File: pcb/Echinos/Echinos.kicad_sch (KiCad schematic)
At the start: 1 part

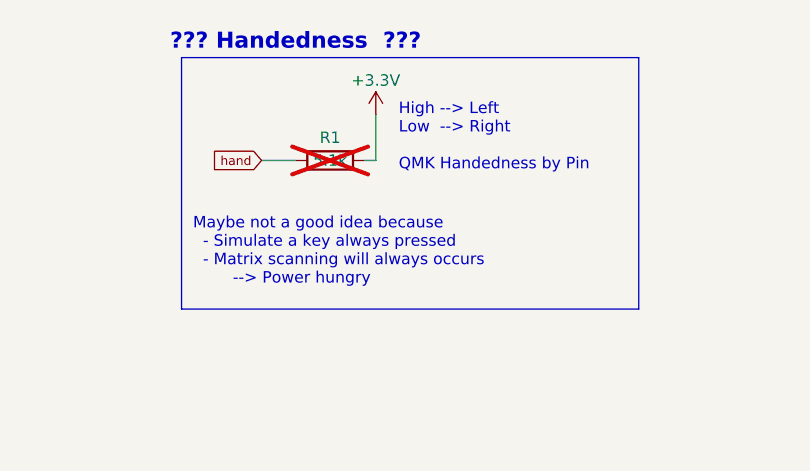
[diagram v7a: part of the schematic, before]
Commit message: [PCB] - Save last state with Gemini MCU board (with mod exposing more pins).
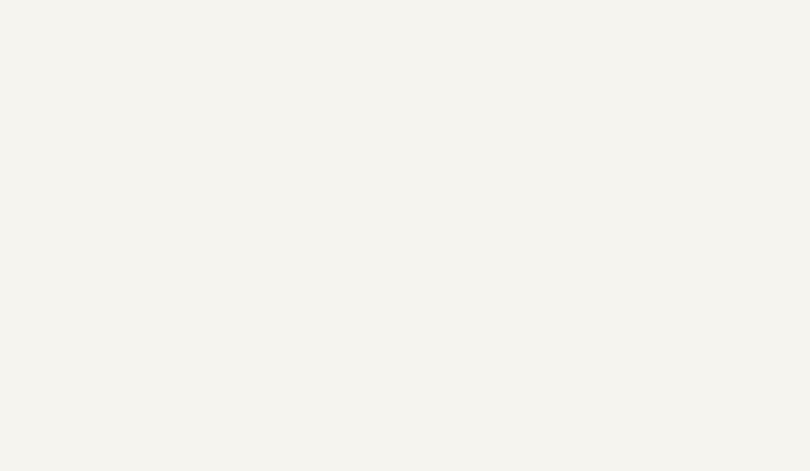
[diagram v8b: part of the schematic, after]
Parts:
- removed R1: 5.1k, Resistor_SMD:R_0402_1005Metric_Pad0.72x0.64mm_HandSolder, symbol Device:R
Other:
- note removed: "??? Handedness ???"
- note removed: "High --> Left Low --> Right QMK Handedness by Pin"
- note removed: "Maybe not a good idea because - Simulate a key always pressed - Matrix scanning will always occurs --> Power hungry"
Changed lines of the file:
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@@
-	)
-	(rectangle
-		(start 154.94 20.32)
-		(end 205.74 48.26)
-		(stroke
-			(width 0)
-			(type default)
-		)
-		(fill
-			(type none)
-		)
 	)
 	(rectangle
@@
 		(fill
 			(type none)
-		)
-	)
-	(text "High --> Left\nLow  --> Right\n\nQMK Handedness by Pin"
-		(exclude_from_sim no)
-		(at 179.07 33.02 0)
-		(effects
-			(font
-				(size 1.27 1.27)
-			)
-			(justify left bottom)
-		)
-	)
-	(text "??? Handedness  ???"
-		(exclude_from_sim no)
-		(at 153.67 19.685 0)
-		(effects
-			(font
-				(size 1.778 1.778)
-				(thickness 0.3556)
-				(bold yes)
-			)
-			(justify left bottom)
 		)
 	)
@@
 		)
 	)
-	(text "Maybe not a good idea because\n  - Simulate a key always pressed\n  - Matrix scanning will always occurs\n		--> Power hungry"
-		(exclude_from_sim no)
-		(at 156.21 45.72 0)
-		(effects
-			(font
-				(size 1.27 1.27)
-			)
-			(justify left bottom)
-		)
-	)
 	(wire
 		(pts
@@
 	(wire
 		(pts
-			(xy 176.53 31.75) (xy 176.53 26.67)
-		)
-		(stroke
-			(width 0)
-			(type default)
-		)
-	)
-	(wire
-		(pts
 			(xy 266.7 44.45) (xy 266.7 34.29)
-		)
-		(stroke
-			(width 0)
-			(type default)
-		)
-	)
-	(wire
-		(pts
-			(xy 163.83 31.75) (xy 167.64 31.75)
 		)
 		(stroke
@@
 		)
 	)
-	(wire
-		(pts
-			(xy 175.26 31.75) (xy 176.53 31.75)
-		)
-		(stroke
-			(width 0)
-			(type default)
-		)
-	)
-	(global_label "hand"
-		(shape input)
-		(at 163.83 31.75 180)
-		(fields_autoplaced yes)
-		(effects
-			(font
-				(size 1 1)
-			)
-			(justify right)
-		)
-		(property "Intersheetrefs" "${INTERSHEET_REFS}"
-			(at 157.9229 31.75 0)
-			(effects
-				(font
-					(size 1.27 1.27)
-				)
-				(justify right)
-				(hide yes)
-			)
-		)
-	)
 	(symbol
 		(lib_id "power:PWR_FLAG")
@@
 	)
 	(symbol
-		(lib_id "Device:R")
-		(at 171.45 31.75 90)
-		(unit 1)
-		(exclude_from_sim yes)
-		(in_bom no)
-		(on_board no)
-		(dnp yes)
-		(property "Reference" "R1"
-			(at 171.45 29.21 90)
-			(effects
-				(font
-					(size 1.27 1.27)
-				)
-			)
-		)
-		(property "Value" "5.1k"
-			(at 171.45 31.75 90)
-			(effects
-				(font
-					(size 1.27 1.27)
-				)
-			)
-		)
-		(property "Footprint" "Resistor_SMD:R_0402_1005Metric_Pad0.72x0.64mm_HandSolder"
-			(at 171.45 33.528 90)
-			(effects
-				(font
-					(size 1.27 1.27)
-				)
-				(hide yes)
-			)
-		)
-		(property "Datasheet" "~"
-			(at 171.45 31.75 0)
-			(effects
-				(font
-					(size 1.27 1.27)
-				)
-				(hide yes)
-			)
-		)
-		(property "Description" ""
-			(at 171.45 31.75 0)
-			(effects
-				(font
-					(size 1.27 1.27)
-				)
-			)
-		)
-		(property "LCSC" "C25905"
-			(at 171.45 31.75 0)
-			(effects
-				(font
-					(size 1.27 1.27)
-				)
-				(hide yes)
-			)
-		)
-		(pin "1"
-		)
-		(pin "2"
-		)
-		(instances
-			(project "Echinos"
-				(path "/5bd3006d-ec09-4ffb-bec3-03fa5613b46a"
-					(reference "R1")
-					(unit 1)
-				)
-			)
-		)
-	)
-	(symbol
 		(lib_id "power:PWR_FLAG")
 		(at 247.65 38.1 180)
@@
 					(unit 1)
 				)
-			)
-		)
-	)
-	(symbol
-		(lib_id "power:+3.3V")
-		(at 176.53 26.67 0)
-		(unit 1)
-		(exclude_from_sim no)
-		(in_bom yes)
-		(on_board yes)
-		(dnp no)
-		(property "Reference" "#PWR01"
-			(at 176.53 30.48 0)
-			(effects
-				(font
-					(size 1.27 1.27)
-				)
-				(hide yes)
-			)
-		)
-		(property "Value" "+3.3V"
-			(at 176.53 22.86 0)
-			(effects
-				(font
-					(size 1.27 1.27)
-				)
-			)
-		)
-		(property "Footprint" ""
-			(at 176.53 26.67 0)
-			(effects
-				(font
-					(size 1.27 1.27)
-				)
-				(hide yes)
-			)
-		)
-		(property "Datasheet" ""
-			(at 176.53 26.67 0)
-			(effects
-				(font
-					(size 1.27 1.27)
-				)
-				(hide yes)
-			)
-		)
-		(property "Description" ""
-			(at 176.53 26.67 0)
-			(effects
-				(font
-					(size 1.27 1.27)
-				)
-			)
-		)
-		(pin "1"
-		)
-		(instances
-			(project "Echinos"
-				(path "/5bd3006d-ec09-4ffb-bec3-03fa5613b46a"
-					(reference "#PWR01")
-					(unit 1)
-				)
